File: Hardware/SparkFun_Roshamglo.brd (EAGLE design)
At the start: 33 x 67.3 mm, 35 parts, among them IC1 ATTINY84A, J1 ICSP, J2 USBPCB, Q1 500mA/300V, U1 IR-Receiver, U3 AP2112K-3.3V

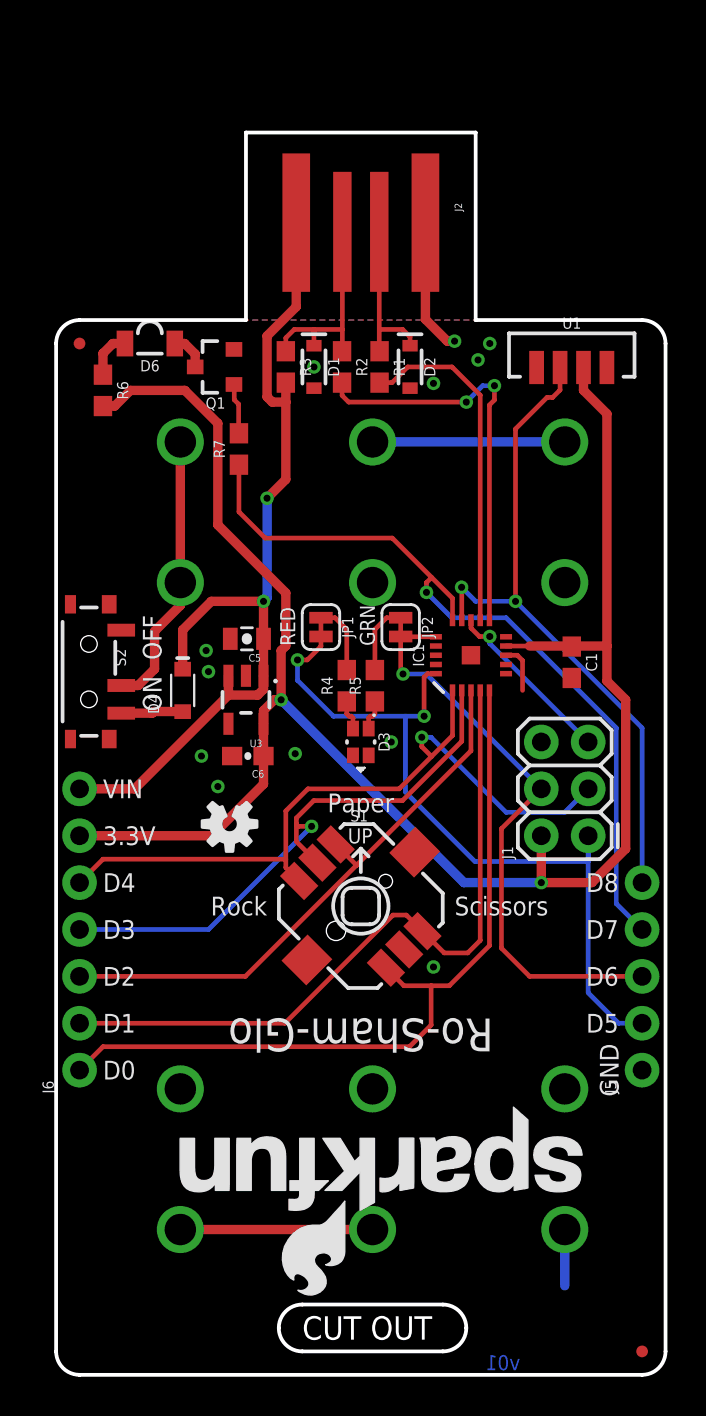
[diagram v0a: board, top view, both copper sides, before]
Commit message: V01 changes
- Fixed version number DRC error
- Added pin 1 marker to Attiny84 to make orientation obvious after
placement.
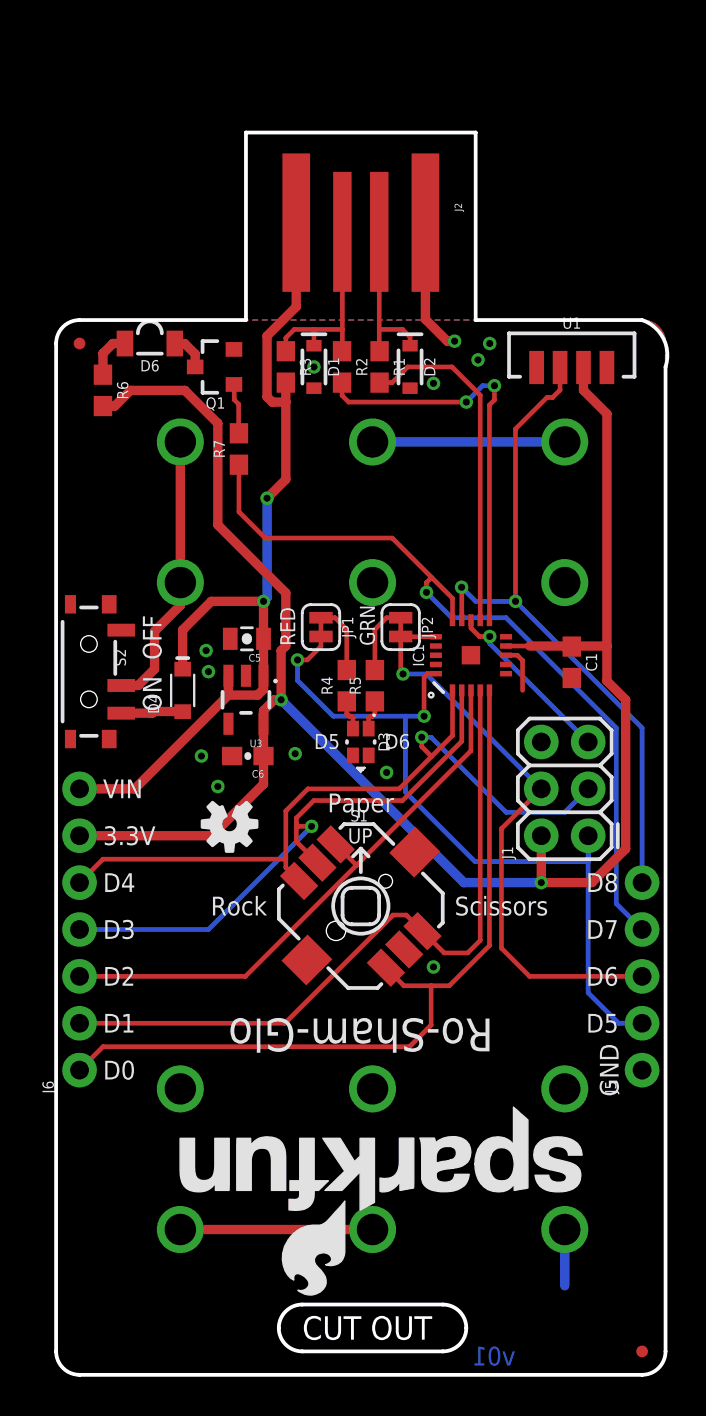
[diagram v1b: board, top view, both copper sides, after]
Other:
- board size 33 x 67.3 mm -> 33.1 x 67.3 mm
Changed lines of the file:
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@@
 <layer number="37" name="tTest" color="7" fill="1" visible="no" active="yes"/>
 <layer number="38" name="bTest" color="7" fill="1" visible="no" active="yes"/>
-<layer number="39" name="tKeepout" color="4" fill="11" visible="no" active="yes"/>
-<layer number="40" name="bKeepout" color="1" fill="11" visible="no" active="yes"/>
+<layer number="39" name="tKeepout" color="4" fill="11" visible="yes" active="yes"/>
+<layer number="40" name="bKeepout" color="1" fill="11" visible="yes" active="yes"/>
 <layer number="41" name="tRestrict" color="4" fill="10" visible="no" active="yes"/>
 <layer number="42" name="bRestrict" color="1" fill="10" visible="no" active="yes"/>
@@
 <layer number="44" name="Drills" color="7" fill="1" visible="no" active="yes"/>
 <layer number="45" name="Holes" color="7" fill="1" visible="yes" active="yes"/>
-<layer number="46" name="Milling" color="3" fill="1" visible="yes" active="yes"/>
-<layer number="47" name="Measures" color="7" fill="1" visible="no" active="yes"/>
+<layer number="46" name="Milling" color="3" fill="1" visible="no" active="yes"/>
+<layer number="47" name="Measures" color="7" fill="1" visible="yes" active="yes"/>
 <layer number="48" name="Document" color="7" fill="1" visible="no" active="yes"/>
 <layer number="49" name="Reference" color="7" fill="1" visible="no" active="yes"/>
@@
 <wire x1="1.27" y1="0" x2="31.75" y2="0" width="0.2032" layer="20"/>
 <wire x1="31.75" y1="0" x2="33.02" y2="1.27" width="0.2032" layer="20" curve="90"/>
-<wire x1="33.02" y1="1.27" x2="33.02" y2="55.88" width="0.2032" layer="20"/>
-<wire x1="33.02" y1="55.88" x2="31.75" y2="57.15" width="0.2032" layer="20" curve="90"/>
+<wire x1="33.02" y1="1.27" x2="33.02" y2="54.61" width="0.2032" layer="20"/>
+<wire x1="33.02" y1="54.61" x2="31.75" y2="57.15" width="0.2032" layer="20" curve="90"/>
 <wire x1="31.75" y1="57.15" x2="22.733" y2="57.15" width="0.2032" layer="20"/>
 <wire x1="10.287" y1="57.15" x2="1.27" y2="57.15" width="0.2032" layer="20"/>
@@
 <text x="16.51" y="30.48" size="1.016" layer="21" font="vector" ratio="15" align="bottom-center">Paper</text>
 <text x="21.59" y="25.4" size="1.016" layer="21" font="vector" ratio="15" align="center-left">Scissors</text>
-<text x="25.146" y="0.254" size="0.8128" layer="16" font="vector" ratio="15" rot="MR0">v01</text>
+<text x="24.892" y="0.508" size="1.016" layer="16" font="vector" ratio="20" rot="MR0">v01</text>
+<text x="13.97" y="33.909" size="0.8128" layer="21" font="vector" ratio="15">D5</text>
+<text x="17.78" y="33.909" size="0.8128" layer="21" font="vector" ratio="15">D6</text>
 </plain>
 <attributes>
@@
 <wire x1="20.01" y1="57.191290625" x2="21.194290625" y2="56.007" width="0.508" layer="1"/>
 <wire x1="21.194290625" y1="56.007" x2="21.59" y2="56.007" width="0.508" layer="1"/>
-<via x="18.161" y="34.29" extent="1-16" drill="0.381"/>
+<via x="17.907" y="32.639" extent="1-16" drill="0.381"/>
 <wire x1="24.379" y1="38.989" x2="24.989021875" y2="38.989" width="0.254" layer="1"/>
 <wire x1="24.989021875" y1="38.989" x2="25.273" y2="38.705021875" width="0.254" layer="1"/>

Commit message: v01 changes
- Extended USB connector length 0.1"
- Added jumpers to pins 7 and 8
- Changed project name silk to single word
- Added PWM pin labels
- Rotated pin names 90 deg
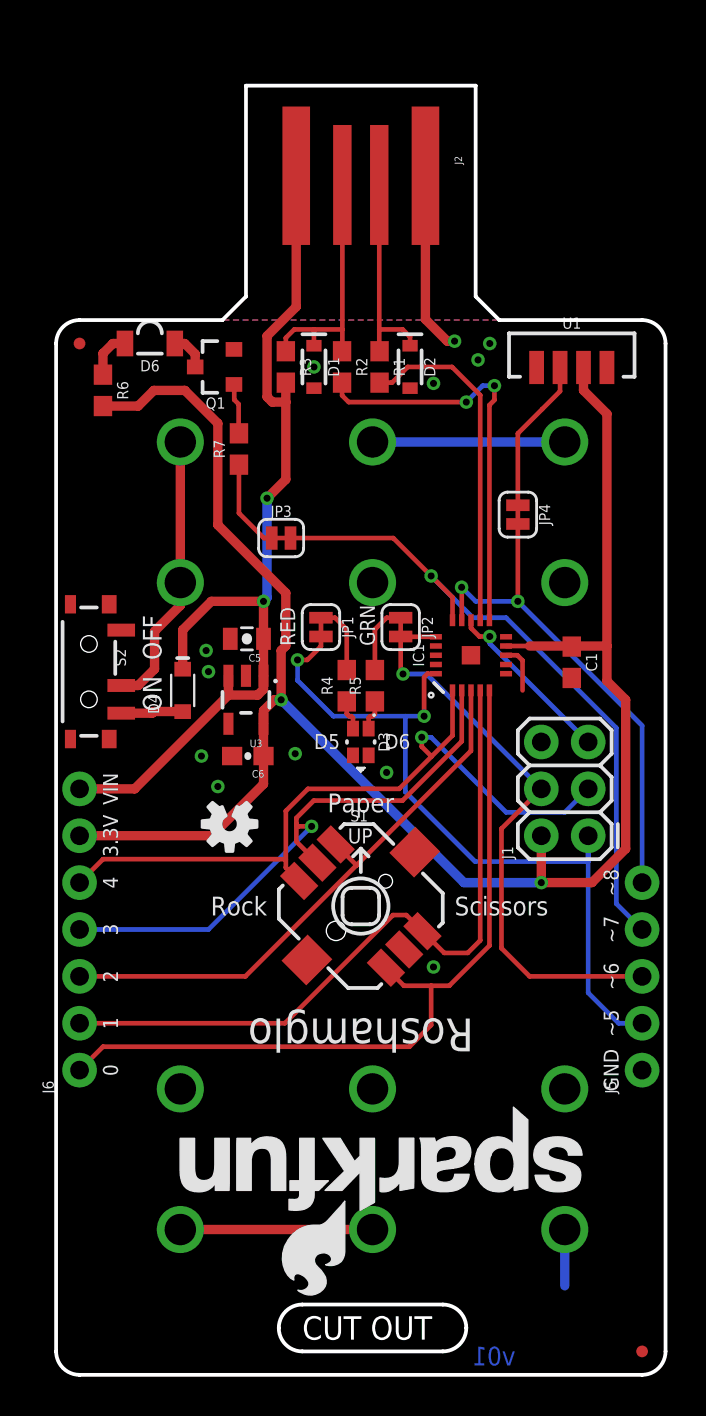
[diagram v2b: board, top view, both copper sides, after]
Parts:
- added JP3, JP4: (no value), SparkFun-Jumpers:SMT-JUMPER_2_NC_TRACE_SILK
- moved J2 2.54 mm to (16.5, 64.8)
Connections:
- new net N$10: JP3.1, R7.1
- new net N$9: JP4.1, U1.3
- net 7: now also JP3.2; no longer R7.1
- net 8: now also JP4.2; no longer U1.3
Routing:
- net 8: track 37.0 -> 27.4 mm
- net N$9: track 0.00 -> 8.41 mm
- net 7: track 43.0 -> 36.3 mm
- net N$10: track 0.00 -> 4.96 mm
- net VIN: track 48.7 -> 51.3 mm
- net GND: track 13.0 -> 15.5 mm
- net D-: track 11.3 -> 13.9 mm
- net D+: track 8.79 -> 11.3 mm
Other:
- board size 33.1 x 67.3 mm -> 33 x 69.8 mm
- board text added: "0"
- board text added: "1"
- board text added: "2"
- board text added: "3"
- board text added: "4"
- board text added: "Roshamglo"
- board text added: "~5"
- board text added: "~6"
- board text added: "~7"
- board text added: "~8"
- board text removed: "D0"
- board text removed: "D1"
- board text removed: "D2"
- board text removed: "D3"
- board text removed: "D4"
- board text removed: "D7"
- board text removed: "D8"
- board text removed: "Ro-Sham-Glo"

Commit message: v01 changes
- Added labels to jumpers
- Cleaned up a couple traces
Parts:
- moved J2 2.54 mm to (16.5, 67.3)
- moved R6 0.89 mm to (3.43, 53.3), turned to 0 degrees
- moved Q1 0.77 mm to (9.40, 54.7), turned to 0 degrees
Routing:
- net GND: track 15.5 -> 18.1 mm, vias 12 -> 13
- net D-: track 13.9 -> 16.4 mm
- net D+: track 11.3 -> 13.9 mm
- net 3.3V: track 98.8 -> 96.7 mm
- net VIN: track 51.3 -> 52.5 mm
- net N$5: track 2.04 -> 3.01 mm
- net N$6: track 2.78 -> 3.67 mm
- net N$1: track 2.56 -> 3.39 mm
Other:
- board size 33 x 69.8 mm -> 33 x 72.4 mm
- board text added: "IR LED"
- board text added: "IR REC."
